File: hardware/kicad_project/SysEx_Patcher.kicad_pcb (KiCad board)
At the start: 4 copper layers, 172 x 172 mm, 99 parts, among them J1 MIDI_IN, J10 JACK6.35, J2 MIDI_OUT, J3 DC_5V, J4 BAT_PWR, J5 OLED, SW2 SW, SW3 SW, SW4 SW, SW5 SW, SW6 SW, SW7 SW, SW8 SW, U1 6N138, U2 CD74HC4067

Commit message: pcb v1.1: empreinte mini-XLR + placement du filtre et du pull-down
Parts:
- added C20: 100nF, Capacitor_THT:C_Disc_D5.0mm_W2.5mm_P5.00mm, F.Cu at (99.0, 182.0)
- added R31: 470k, Resistor_THT:R_Axial_DIN0207_L6.3mm_D2.5mm_P10.16mm_Horizontal, F.Cu at (108.0, 182.0)
- added R32: 1k, Resistor_THT:R_Axial_DIN0207_L6.3mm_D2.5mm_P10.16mm_Horizontal, F.Cu at (86.0, 182.0)
- J10: value JACK6.35 -> MINI-XLR-5; footprint Connector_Audio:Jack_6.35mm_Neutrik_NRJ6HF-1_Horizontal -> Connector_Audio:MiniXLR-5_Switchcraft_TRAPC_Horizontal
- moved J10 7.28 mm to (107.0, 40.0), turned to 180 degrees

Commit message: pcb v1.1: routage complet du canal switch (0 connexion manquante)
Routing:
- net SW_BEND: track 0.00 -> 152.1 mm
- net MUX_CH2: track 0.00 -> 45.1 mm
- net D26: track 132.7 -> 155.6 mm, vias 0 -> 1
- net D27: track 121.9 -> 143.0 mm, vias 0 -> 1
- net D11: track 158.7 -> 177.5 mm
- net A0: track 96.6 -> 79.6 mm, vias 1 -> 0
- net D6: track 142.0 -> 125.5 mm, vias 2 -> 1
- net VIN_RAW: track 201.9 -> 187.7 mm
- net D3: track 109.5 -> 96.3 mm
- net D8: track 152.9 -> 162.6 mm, vias 1 -> 0
- net A12: track 116.3 -> 108.1 mm
- net A2: track 28.5 -> 36.4 mm
- net A1: track 59.0 -> 53.5 mm, vias 1 -> 0
- net A9: track 78.0 -> 83.5 mm, vias 1 -> 0
- net D20_SDA: track 151.4 -> 146.0 mm
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
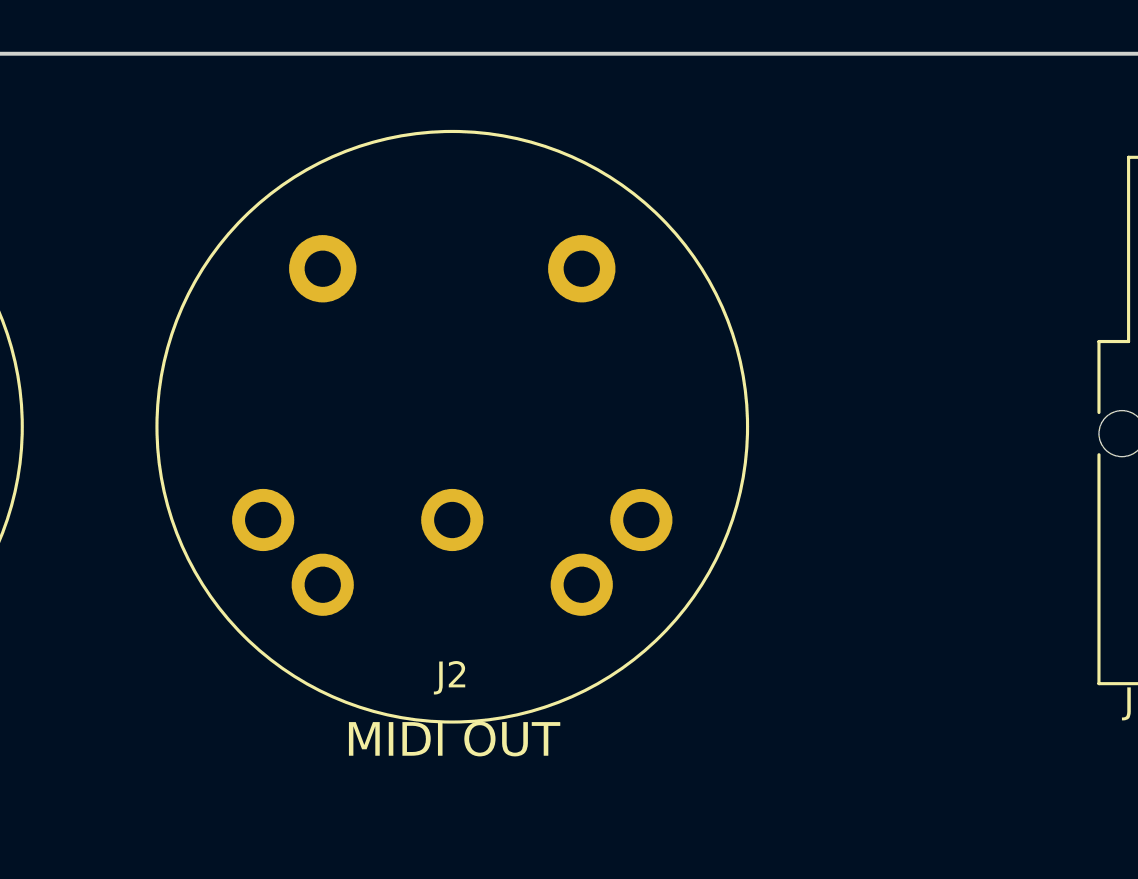
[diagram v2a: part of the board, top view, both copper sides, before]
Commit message: pcb v1.1: écarte les embases MIDI à 37mm d'entraxe + re-routage complet
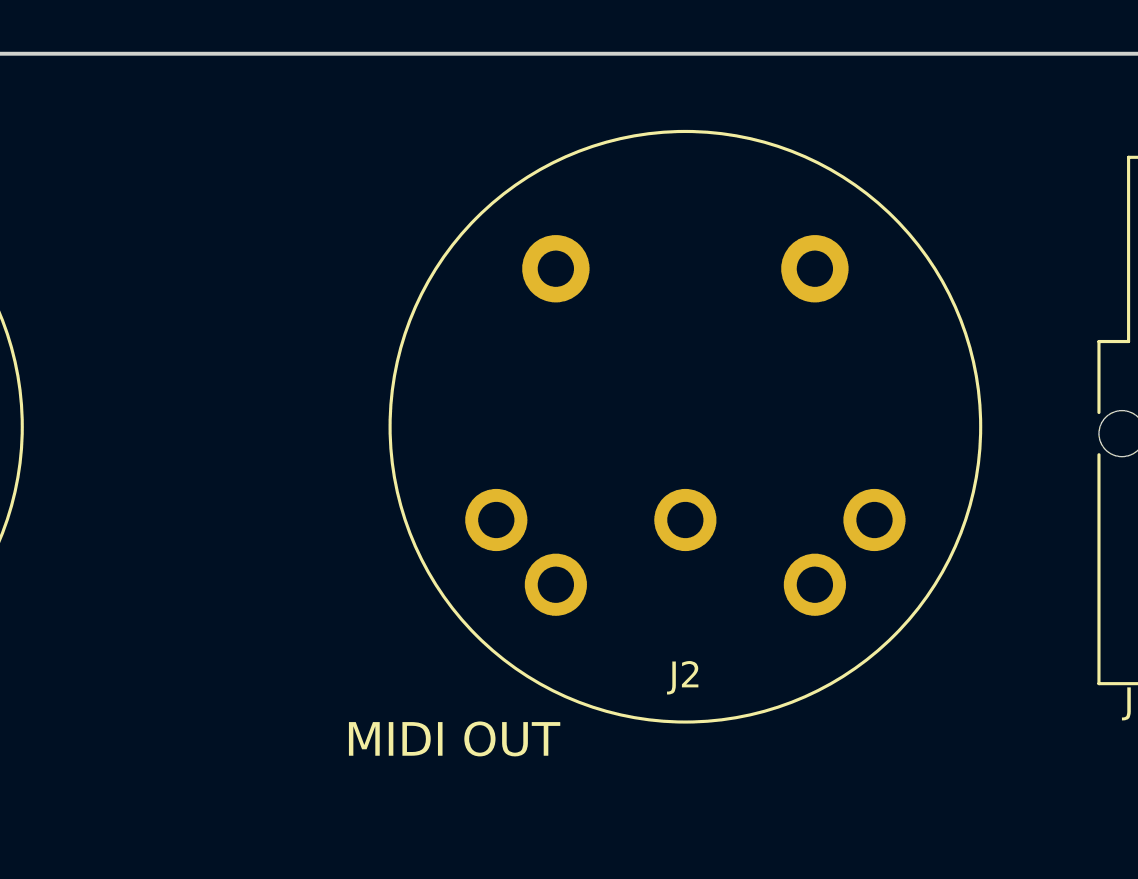
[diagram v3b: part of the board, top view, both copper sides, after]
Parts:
- moved J2 9.00 mm to (81.0, 38.0)
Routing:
- net MIDI_OUT_5: track 35.9 -> 32.1 mm
- net MIDI_OUT_4: track 25.7 -> 22.0 mm
